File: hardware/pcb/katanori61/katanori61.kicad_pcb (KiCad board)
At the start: 4 copper layers, 82 x 37.4 mm, 59 parts, among them J1 XIAO RISER, J10 BAT (JST-PH), J13 USB-C, J2 OLED, J4 SPK IN, J5 SPK OUT, J6 BTN2, J7 REED+TOGGLE, K31 G6S-2F DC5, Q1 MMUN2133LT1G, Q2 AO3401A, Q31 SS8050, U1 TPS61090RSAR, U2 MCP73871-2CCI/ML, U3 INA226AIDGSR, U4 AS5600-ASOM

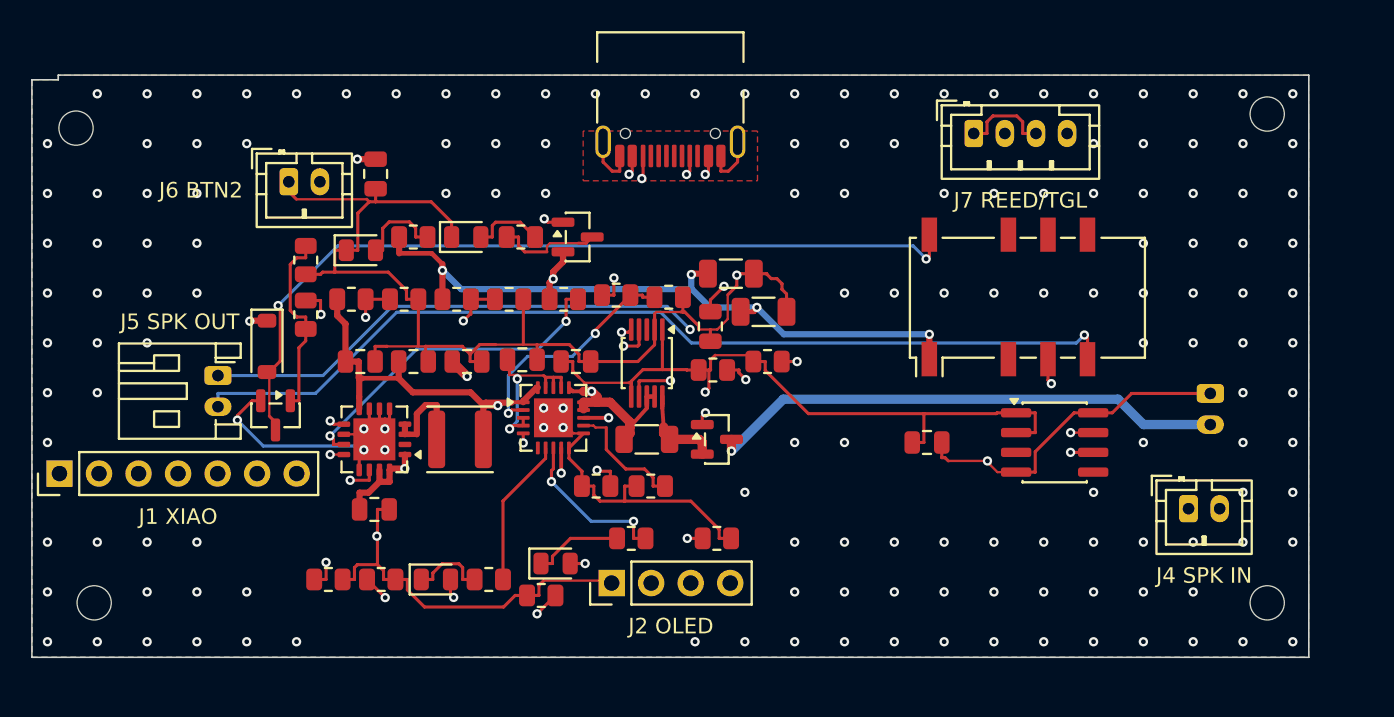
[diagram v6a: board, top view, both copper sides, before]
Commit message: pcb v6.1: C6・C9（47µF）を U1 の足元へ
🔒 ユーザー 2026-09-17「C6・C9 を U1 の足元へ寄せてくださいな」。

Y 23.0 の列（板 X 44.0 / 47.0）に居て、U1 の V5 ピン（15 番）から銅で 33.24mm / 37.18mm
＝ 42.3 / 47.7 mΩ 離れていた。600kHz では配線のインダクタンス（33mm で 30nH ≒ 120mΩ）が
効くので、47µF が **出力リプルに対して働いていなかった**。

U1 の下の辺（V5 の 15・16 番・板 Y 12.04）の真下、C2 の隣へ 3 本並べた（1206 なので間隔 3.5）。
  C2  板 X 22.0   4.2 → 6.0 mΩ
  C6  板 X 25.5  42.3 → 3.3 mΩ（33.24 → 2.56mm）
  C9  板 X 29.0  47.7 → 10.8 mΩ（37.18 → 7.53mm）

⚠ 別セッションが「U1 の V5 から 174mΩ」と報告していたが、この板では 42〜48mΩ だった
  （並べ直す前か 4 層にする前の板の値と思われる）。結論の向きは合っていたので直した。
  なお XIAO（J1）から見ると C2 も C6 も 75mΩ 台で差が無く、ゆっくりした負荷変動に対しては
  元の位置でも働いていた。発注を止める話ではなかった。

■ ついでに減ったもの

U2 の 9 番（VBUS）の逃げ道（escape_stub）が要らなくなった。4 層とこの配置なら自動配線が
自分で通す。手で引く線はケルビンの 2 本と PROG1 の 1 本だけになった。

■ 検算

未接続 0 ／ 回路図との差 0 ／ DRC エラー 0 ／ 銅のすきま 下回り 0。
警告は lib_footprint_mismatch 4 件（留め穴・既知）だけ。
模型（v61_parts.scad 56 個）と STL も板に合わせて出し直した。

CPL とガーバーは別セッションが 04:15 にこの板から作り直した物が入っている
（JLCPCB 向けの回転補正つき・48 個・負の角度 0 件）。
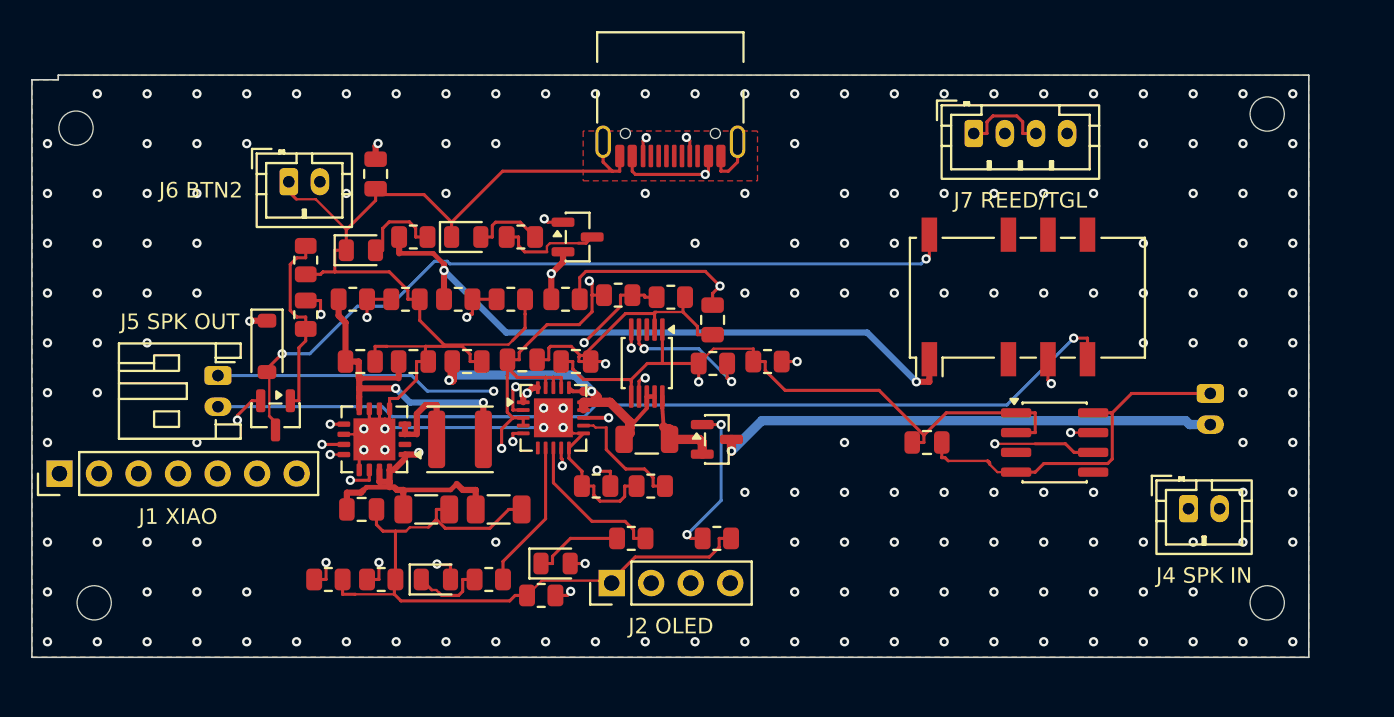
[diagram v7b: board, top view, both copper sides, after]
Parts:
- C4: renamed from C8; value 10uF -> 0.1uF
- C41: renamed from R43; value 10K -> 0.1uF; footprint Resistor_SMD:R_0805_2012Metric -> Capacitor_SMD:C_0805_2012Metric
- C6: renamed from R16; value 1.0K -> 47uF; footprint Resistor_SMD:R_0805_2012Metric -> Capacitor_SMD:C_1206_3216Metric
- C7: renamed from C41; value 0.1uF -> 10uF
- C8: renamed from R42; value 10K -> 10uF; footprint Resistor_SMD:R_0805_2012Metric -> Capacitor_SMD:C_0805_2012Metric
- C9: renamed from R17; value 100K -> 47uF; footprint Resistor_SMD:R_0805_2012Metric -> Capacitor_SMD:C_1206_3216Metric
- R13: renamed from R7; value 82K -> 200K
- R16: renamed from C1; value 10uF -> 1.0K; footprint Capacitor_SMD:C_0805_2012Metric -> Resistor_SMD:R_0805_2012Metric
- R17: renamed from C4; value 0.1uF -> 100K; footprint Capacitor_SMD:C_0805_2012Metric -> Resistor_SMD:R_0805_2012Metric
- R2: renamed from R4; value 200K -> 330K
- R3: renamed from R13; value 200K -> 1.87M
- R4: renamed from R6; value 220K -> 200K
- R42: renamed from R1; value 1.87M -> 10K
- R43: renamed from R2; value 330K -> 10K
- R6: renamed from C6; value 47uF -> 220K; footprint Capacitor_SMD:C_1206_3216Metric -> Resistor_SMD:R_0805_2012Metric
- R7: renamed from C9; value 47uF -> 82K; footprint Capacitor_SMD:C_1206_3216Metric -> Resistor_SMD:R_0805_2012Metric
- moved R43 23.7 mm to (87.3, 58.4)
- moved R42 23.6 mm to (83.7, 58.5)
- moved R17 17.2 mm to (79.8, 66.4)
- moved R16 17.1 mm to (76.2, 66.4)
- moved C41 12.3 mm to (74.9, 58.4)
- moved C8 12.3 mm to (71.5, 58.3)
- moved C6 11.0 mm to (65.3, 67.9)
- moved C9 9.89 mm to (70.0, 67.9)
- moved R6 7.37 mm to (77.7, 54.1)
- moved C4 6.99 mm to (64.5, 58.4)
- moved C7 6.99 mm to (68.0, 58.4)
- moved C1 6.86 mm to (61.1, 58.4)
- moved R3 6.78 mm to (67.4, 54.4)
- moved R4 6.78 mm to (70.8, 54.4)
- moved R1 6.67 mm to (60.6, 54.4)
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- renumbered C7 to C1, R3 to R1
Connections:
- C1 pad 1: VLIPO -> VSYS
- C4 pad 1: VBUS -> VSYS
- C41 pad 2: SCL -> GND
- C6 pad 1: GND -> V5
- C6 pad 2: PROG1 -> GND
- C7 pad 1: V33 -> VLIPO
- C8 pad 1: V33 -> VBUS
- C8 pad 2: SDA -> GND
- C9 pad 1: GND -> V5
- C9 pad 2: PROG3 -> GND
- R1 pad 1: V5 -> VSYS
- R1 pad 2: FB -> LBI
- R13 pad 1: VPCC -> VSYS
- R13 pad 2: GND -> EN
- R16 pad 1: VSYS -> GND
- R16 pad 2: GND -> PROG1
- R17 pad 1: VSYS -> GND
- R17 pad 2: GND -> PROG3
- R2 pad 1: FB -> LBI
- R3 pad 1: VSYS -> V5
- R3 pad 2: EN -> FB
- R4 pad 1: VBUS -> FB
- R4 pad 2: VPCC -> GND
- R42 pad 1: VSYS -> V33
- R42 pad 2: LBI -> SDA
- R43 pad 1: LBI -> V33
- R43 pad 2: GND -> SCL
- R6 pad 1: V5 -> VBUS
- R6 pad 2: GND -> VPCC
- R7 pad 1: V5 -> VPCC
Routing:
- net EN: track 60.7 -> 88.3 mm, vias 3 -> 2
- net SCL: track 94.6 -> 85.3 mm
- net V5: track 109.1 -> 118.4 mm, vias 7 -> 5
- net LBO: track 35.9 -> 27.1 mm
- net GND: track 297.1 -> 303.6 mm, vias 160 -> 172
- net FB: track 26.9 -> 20.7 mm
- net CC2: track 36.9 -> 41.4 mm
- net SPKM: track 75.4 -> 71.4 mm
- net SDA: track 89.6 -> 86.0 mm
- net CC1: track 42.8 -> 46.1 mm
- net COL: track 53.9 -> 51.2 mm
- net V33: track 98.1 -> 96.2 mm
- net SPKO: track 61.3 -> 59.6 mm
- net VLIPO: track 20.3 -> 21.7 mm
- net BATRAW: track 33.6 -> 32.4 mm
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
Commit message: v6.1: USB-C を素の 4 本足へ戻す（胴の出 1.3）／レジンのハッチは口のまわりを 1.2 掘る
🔒 ユーザー 2026-09-17「1.3 以下に戻してレジンのハッチは口の周りを掘るしかないね。
何ミリにする？とか聞かれてもわからんので、そこは任せたい」。

■ なぜ戻すか

直前のコミットで胴の出を 2.5（レジン基準）にしたが、そのとき **シェルの足が 2 本のまま
確定することを言っていなかった**。前寄りの足はパッドの外縁が口の面から 1.800 後ろにあり、
2.5 出すと板の縁の 0.500 外へはみ出す。自作の NoFrontLegs は v6（出 3.0）のための物で、
PCB-V61.md 212 行は「v6.1 は 1.53 出しなので素の足跡が使える」と書いていた。
その名残を根拠にして 2.5 を通していた。

■ 直した内容

  胴の出 2.5 → **1.3**（v61_board.usbc_out() を HATCH_T_NYLON 基準へ）
  足形     katanori:…_NoFrontLegs → **Connector_USB:USB_C_Receptacle_HRO_TYPE-C-31-M-12**
           一番縁寄りのパッドの外縁は板の縁の 0.500 内側。抜き挿しの力を足 4 本で受ける。
  PCB_Y0 / PCB_HATCH_GAP  ナイロン専用の 13.1 / 0.9 をやめて素の 13.5 / 0.5 へ
           （出が 1.3 ならナイロンはそのまま奥まり 0.8。材料で変える必要が無い）

■ レジンのハッチの掘り込み（数字はこちらで決めた）

  深さ 1.2 … 残り肉 1.6 ＝ ナイロンと同じ厚み。奥まりが 2.0 → 0.8 になり両材料で揃う
  大きさ 12.54 × 6.86 … 口の穴（9.54 × 3.86）＋ 片側 1.5。
    ⚠ 出どころは CASE-V2.md 1036 行の前例「口の外形＋余白 1.5」。**プラグの
      オーバーモールドの実寸は手元に無い。**現物が来たら測って詰めること。

■ 回転の補正表（fab.py・別セッションの作りに 1 行足した）

足形の名前が変わったので JLC_ROT が止まった（表に無い足形で止まる作りは正しく働いた）。
NoFrontLegs の行に「元の名前なら表の 180 に当たる」と書いてあったとおり、素の名前へ
差し替えて 📄 の出どころにした。J13 の CPL 角度は 180。

■ 検算

未接続 0 ／ 回路図との差 0 ／ DRC エラー 0 ／ 銅のすきま 下回り 0。
奥まりは ナイロン 0.80 ／ レジン 0.80（掘り込み込み）。
筐体（nylon）: hit_hub 0 ／ hit_knob 0 ／ sk_hub 0。
模型・STL・ガーバー・BOM・CPL も板に合わせて出し直した。

⚠ レジンの sk_hub は 12.59mm³ 当たるが、**HEAD でも同じ**で前からの物。別件として残す。
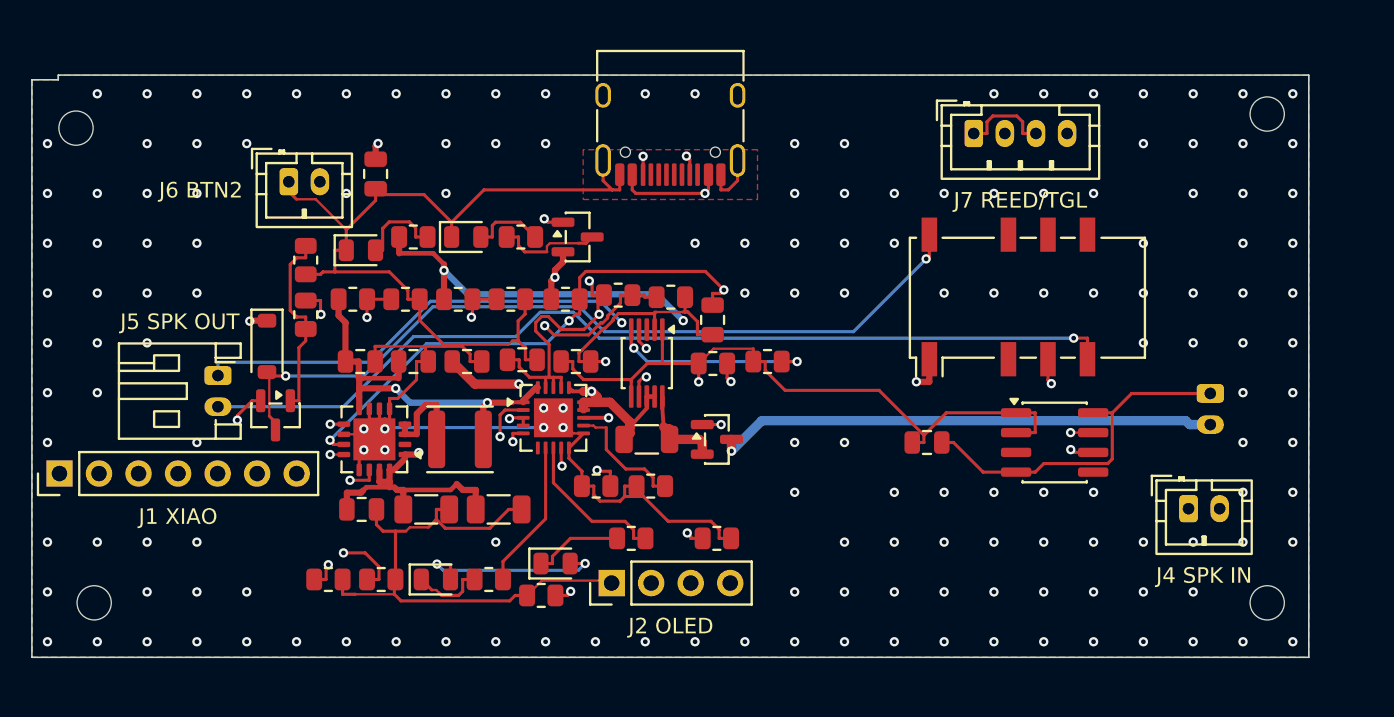
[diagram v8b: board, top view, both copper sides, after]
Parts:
- J13: footprint katanori:USB_C_HRO_TYPE-C-31-M-12_NoFrontLegs -> Connector_USB:USB_C_Receptacle_HRO_TYPE-C-31-M-12
- moved ? 82.4 mm to (119.4, 73.9)
- moved ? 81.6 mm to (119.4, 42.5)
- moved ? 76.5 mm to (42.8, 43.4)
- moved ? 75.4 mm to (44.0, 73.9)
- moved J13 1.20 mm to (81.0, 42.4)
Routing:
- net EN: track 88.3 -> 60.3 mm, vias 2 -> 3
- net SCL: track 85.3 -> 95.4 mm
- net VBUS: track 65.6 -> 73.1 mm, vias 6 -> 7
- net VPCC: track 14.3 -> 21.4 mm
- net BATG: track 10.3 -> 17.2 mm
- net SDA: track 86.0 -> 92.6 mm
- net CC1: track 46.1 -> 40.5 mm
- net CC2: track 41.4 -> 39.0 mm
- net SPKM: track 71.4 -> 73.6 mm
- net GND: track 303.6 -> 305.8 mm, vias 172 -> 165
- net VLIPO: track 21.7 -> 20.3 mm
- net COL: track 51.2 -> 52.3 mm
- net SPKO: track 59.6 -> 60.4 mm
- net VSYS: track 40.5 -> 39.7 mm, vias 4 -> 3
- net V5: vias 5 -> 6
